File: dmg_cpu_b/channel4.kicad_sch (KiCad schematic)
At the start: 104 parts

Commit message: Further fixes made based on raised issues.
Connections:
- net CH4_EG_STOP: now also EROX.2 (~{Q}); no longer EROX.3 (Q)
- net CH4_FEN renamed CH4_FDIS
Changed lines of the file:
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@@
   (junction (at 201.93 281.305) (diameter 0) (color 0 0 0 0)
   )
-  (no_connect (at 403.86 163.195))
+  (no_connect (at 403.86 158.115))
   (no_connect (at 378.46 163.195))
   (no_connect (at 168.91 276.86))
@@
     (stroke (width 0) (type default) (color 0 0 0 0))
   )
-  (wire (pts (xy 403.86 158.115) (xy 406.4 158.115))
+  (wire (pts (xy 403.86 163.195) (xy 406.4 163.195))
     (stroke (width 0) (type default) (color 0 0 0 0))
   )
@@
     (stroke (width 0) (type default) (color 0 0 0 0))
   )
-  (wire (pts (xy 406.4 158.115) (xy 406.4 135.255))
+  (wire (pts (xy 406.4 135.255) (xy 406.4 163.195))
     (stroke (width 0) (type default) (color 0 0 0 0))
   )
@@
     (effects (font (size 1.27 1.27)) (justify right))
   )
-  (hierarchical_label "CH4_FEN" (shape input) (at 25.4 208.915 180)
+  (hierarchical_label "CH4_FDIS" (shape input) (at 25.4 208.915 180)
     (effects (font (size 1.27 1.27)) (justify right))
   )

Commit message: Fixes made based on raised issues (in APU sheets).
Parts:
- added GYBA: INVERTER_A, symbol DMG_CPU_Cells:INVERTER_A
- renumbered DEMA to DEMO
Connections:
- net CH4_1MHz: now also GYBA.1; no longer GARY.1 (CLK)
- net CH4_EG_STOP: now also EROX.3 (Q); no longer EROX.2 (~{Q})
- net ~{FF21_D0}: no longer JYCO.5 (D)
- net ~{FF21_D1}: no longer JYRE.5 (D)
- net ~{FF21_D2}: no longer JYFU.5 (D)
- net at EVUR.1: now also DARO.6; no longer DUBO.2
- net at EVUR.2: now also DUBO.2; no longer DARO.6
- new net: GARY.1 (CLK), GYBA.2
- new net ~{FF22_D0}: JYCO.5 (D)
- new net ~{FF22_D1}: JYRE.5 (D)
- new net ~{FF22_D2}: JYFU.5 (D)
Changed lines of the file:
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@@
   (junction (at 193.04 214.63) (diameter 0) (color 0 0 0 0)
   )
-  (junction (at 128.905 192.405) (diameter 0) (color 0 0 0 0)
-  )
   (junction (at 377.19 81.28) (diameter 0) (color 0 0 0 0)
   )
@@
   (junction (at 80.645 224.155) (diameter 0) (color 0 0 0 0)
   )
+  (junction (at 114.935 184.15) (diameter 0) (color 0 0 0 0)
+  )
   (junction (at 198.12 137.16) (diameter 0) (color 0 0 0 0)
   )
@@
   (junction (at 201.93 281.305) (diameter 0) (color 0 0 0 0)
   )
-  (no_connect (at 403.86 158.115))
+  (no_connect (at 403.86 163.195))
   (no_connect (at 378.46 163.195))
   (no_connect (at 168.91 276.86))
@@
     (stroke (width 0) (type default) (color 0 0 0 0))
   )
-  (wire (pts (xy 403.86 163.195) (xy 406.4 163.195))
+  (wire (pts (xy 403.86 158.115) (xy 406.4 158.115))
     (stroke (width 0) (type default) (color 0 0 0 0))
   )
@@
     (stroke (width 0) (type default) (color 0 0 0 0))
   )
-  (wire (pts (xy 406.4 135.255) (xy 406.4 163.195))
+  (wire (pts (xy 406.4 135.255) (xy 406.4 158.115))
     (stroke (width 0) (type default) (color 0 0 0 0))
   )
-  (wire (pts (xy 131.445 206.375) (xy 128.905 206.375))
+  (wire (pts (xy 131.445 206.375) (xy 130.175 206.375))
     (stroke (width 0) (type default) (color 0 0 0 0))
   )
@@
     (stroke (width 0) (type default) (color 0 0 0 0))
   )
+  (wire (pts (xy 114.935 184.15) (xy 114.935 197.485))
+    (stroke (width 0) (type default) (color 0 0 0 0))
+  )
   (wire (pts (xy 203.2 132.08) (xy 205.74 132.08))
     (stroke (width 0) (type default) (color 0 0 0 0))
@@
     (stroke (width 0) (type default) (color 0 0 0 0))
   )
-  (wire (pts (xy 128.905 192.405) (xy 156.845 192.405))
-    (stroke (width 0) (type default) (color 0 0 0 0))
-  )
   (wire (pts (xy 84.455 238.76) (xy 59.055 238.76))
     (stroke (width 0) (type default) (color 0 0 0 0))
@@
     (stroke (width 0) (type default) (color 0 0 0 0))
   )
+  (wire (pts (xy 114.935 184.15) (xy 156.845 184.15))
+    (stroke (width 0) (type default) (color 0 0 0 0))
+  )
   (wire (pts (xy 62.23 274.32) (xy 62.23 281.305))
     (stroke (width 0) (type default) (color 0 0 0 0))
@@
     (stroke (width 0) (type default) (color 0 0 0 0))
   )
+  (wire (pts (xy 156.845 184.15) (xy 156.845 192.405))
+    (stroke (width 0) (type default) (color 0 0 0 0))
+  )
   (wire (pts (xy 309.88 180.34) (xy 314.96 180.34))
     (stroke (width 0) (type default) (color 0 0 0 0))
@@
     (stroke (width 0) (type default) (color 0 0 0 0))
   )
-  (wire (pts (xy 128.905 192.405) (xy 125.095 192.405))
+  (wire (pts (xy 113.665 184.15) (xy 114.935 184.15))
     (stroke (width 0) (type default) (color 0 0 0 0))
   )
@@
     (stroke (width 0) (type default) (color 0 0 0 0))
   )
+  (wire (pts (xy 116.205 197.485) (xy 114.935 197.485))
+    (stroke (width 0) (type default) (color 0 0 0 0))
+  )
   (wire (pts (xy 136.525 67.31) (xy 136.525 93.345))
     (stroke (width 0) (type default) (color 0 0 0 0))
@@
     (stroke (width 0) (type default) (color 0 0 0 0))
   )
-  (wire (pts (xy 128.905 206.375) (xy 128.905 192.405))
+  (wire (pts (xy 130.175 206.375) (xy 130.175 197.485))
     (stroke (width 0) (type default) (color 0 0 0 0))
   )
@@
     (stroke (width 0) (type default) (color 0 0 0 0))
   )
+  (wire (pts (xy 130.175 197.485) (xy 128.905 197.485))
+    (stroke (width 0) (type default) (color 0 0 0 0))
+  )
   (wire (pts (xy 123.825 28.575) (xy 123.825 33.02))
     (stroke (width 0) (type default) (color 0 0 0 0))
@@
     (effects (font (size 1.27 1.27)) (justify left bottom))
   )
-  (label "~{FF21_D0}" (at 67.945 226.695 0)
+  (label "~{FF22_D0}" (at 67.945 226.695 0)
     (effects (font (size 1.27 1.27)) (justify left bottom))
   )
@@
     (effects (font (size 1.27 1.27)) (justify left bottom))
   )
-  (label "~{FF21_D1}" (at 67.945 209.55 0)
+  (label "~{FF22_D1}" (at 67.945 209.55 0)
     (effects (font (size 1.27 1.27)) (justify left bottom))
   )
@@
     (effects (font (size 1.27 1.27)) (justify left bottom))
   )
-  (label "~{FF21_D2}" (at 69.215 192.405 0)
+  (label "~{FF22_D2}" (at 69.215 192.405 0)
     (effects (font (size 1.27 1.27)) (justify left bottom))
   )
@@
     (effects (font (size 1.27 1.27)) (justify right))
   )
-  (hierarchical_label "~{FF22_D[0..7]}" (shape input) (at 170.815 129.54 180)
+  (hierarchical_label "~{FF22_D[0..6]}" (shape input) (at 170.815 129.54 180)
     (effects (font (size 1.27 1.27)) (justify right))
   )
-  (hierarchical_label "CH4_1MHz" (shape input) (at 125.095 192.405 180)
+  (hierarchical_label "CH4_1MHz" (shape input) (at 113.665 184.15 180)
     (effects (font (size 1.27 1.27)) (justify right))
   )
@@
     (pin "6")
   )
-  (symbol (lib_id "DMG_CPU_Cells:OR_2") (at 350.52 163.195 0) (unit 1)
+  (symbol (lib_id "DMG_CPU_Cells:OR_2") (at 350.52 163.195 0) (mirror x) (unit 1)
     (in_bom yes) (on_board yes) (fields_autoplaced)
     (property "Reference" "EVUR" (id 0) (at 350.5198 155.6852 0))
@@
       (effects (font (size 1.27 1.27)) hide)
     )
-    (property "Datasheet" "http://iceboy.a-singer.de/doc/dmg_cells.html#or2" (id 3) (at 350.52 170.815 0)
+    (property "Datasheet" "http://iceboy.a-singer.de/doc/dmg_cells.html#or2" (id 3) (at 350.52 155.575 0)
       (effects (font (size 1.27 1.27)) hide)
     )
@@
   (symbol (lib_id "DMG_CPU_Cells:DFFR_B2") (at 121.285 95.885 0) (unit 1)
     (in_bom yes) (on_board yes) (fields_autoplaced)
-    (property "Reference" "DEMA" (id 0) (at 121.285 87.8672 0))
+    (property "Reference" "DEMO" (id 0) (at 121.285 87.8672 0))
     (property "Value" "DFFR_B2" (id 1) (at 121.285 90.4041 0))
     (property "Footprint" "" (id 2) (at 121.285 95.885 0)
@@
     (pin "4")
   )
+  (symbol (lib_id "DMG_CPU_Cells:INVERTER_A") (at 122.555 197.485 0) (unit 1)
+    (in_bom yes) (on_board yes)
+    (property "Reference" "GYBA" (id 0) (at 122.555 189.9752 0))
+    (property "Value" "INVERTER_A" (id 1) (at 122.555 192.5121 0))
+    (property "Footprint" "" (id 2) (at 120.015 197.485 0)
+      (effects (font (size 1.27 1.27)) hide)
+    )
+    (property "Datasheet" "http://iceboy.a-singer.de/doc/dmg_cells.html#inv_a" (id 3) (at 123.825 205.105 0)
+      (effects (font (size 1.27 1.27)) hide)
+    )
+    (pin "1")
+    (pin "2")
+  )
   (symbol (lib_id "DMG_CPU_Cells:INVERTER_A") (at 25.4 271.78 0) (unit 1)

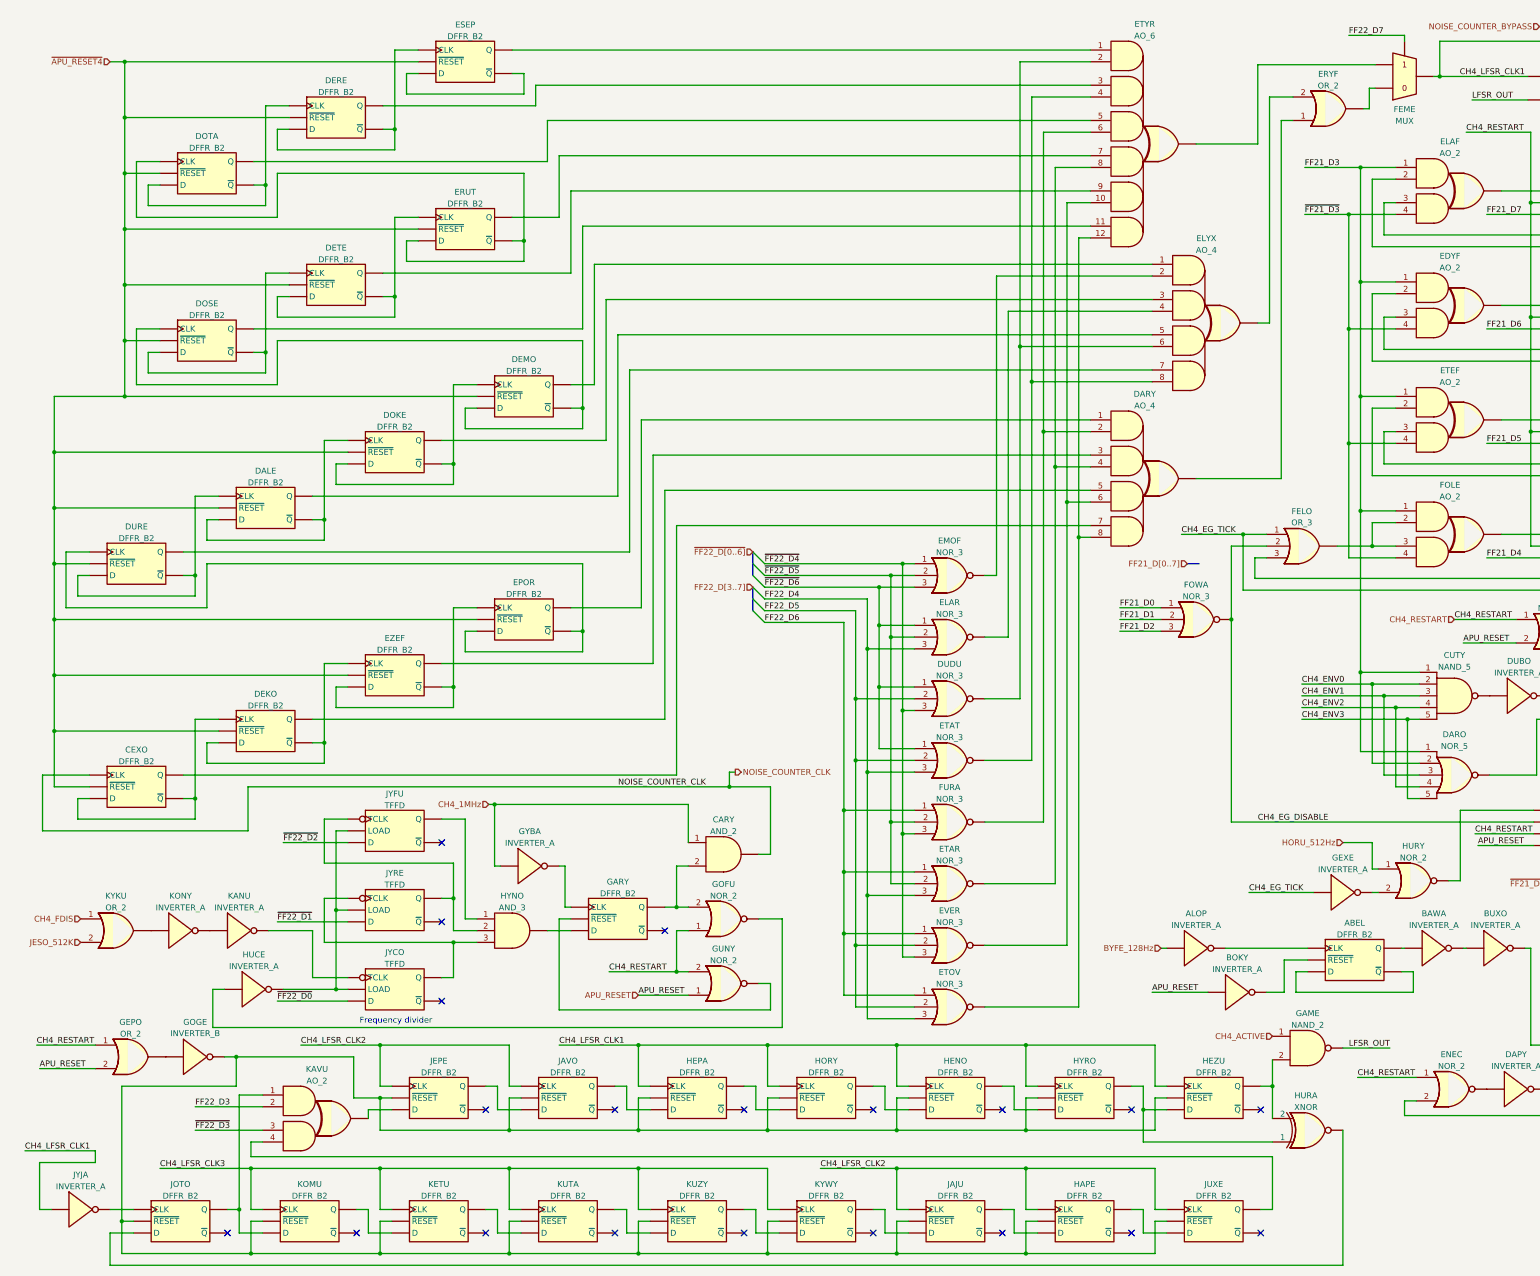
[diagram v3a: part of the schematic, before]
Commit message: Some mistakes found in APU sheets, notes added for clarity. Edit in PPU sheets following review.
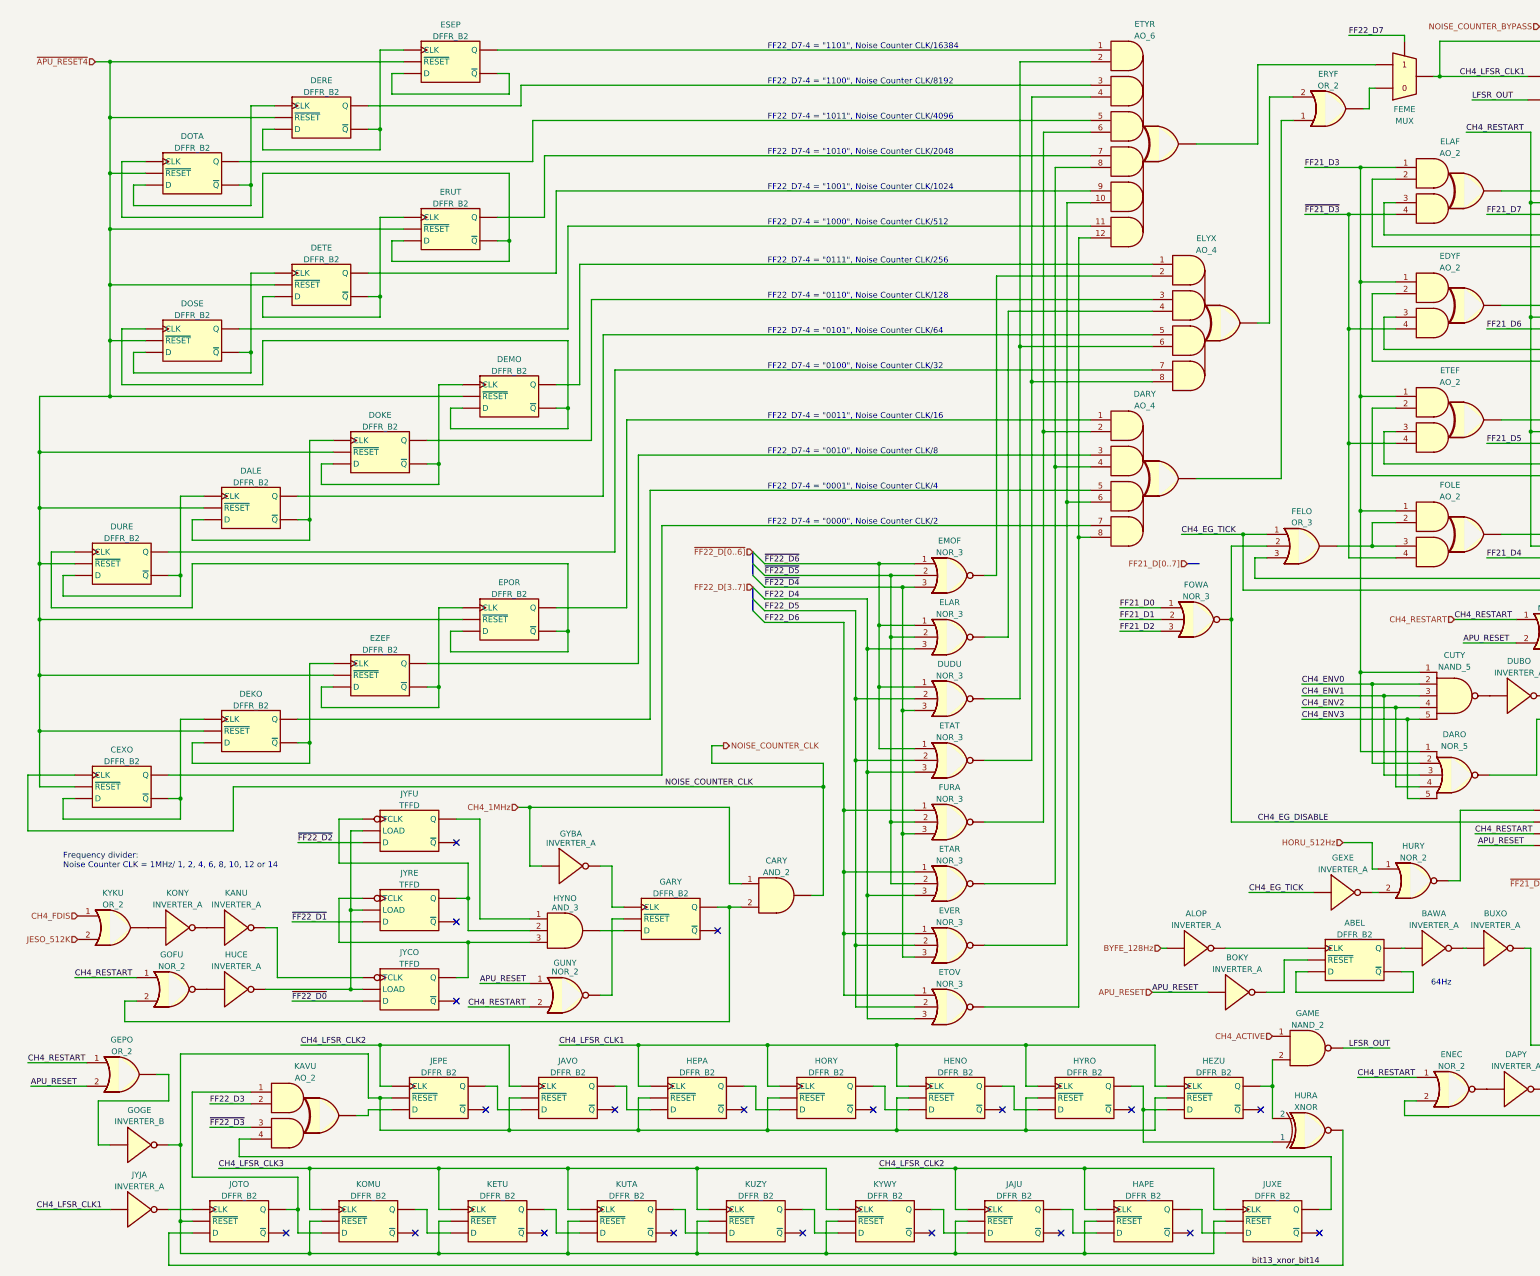
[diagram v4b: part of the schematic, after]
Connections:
- net ~{FF22_D4}: now also EMOF.3; no longer EMOF.1
- net ~{FF22_D6}: now also EMOF.1; no longer EMOF.3
- net bit13_xnor_bit14: now reaches HURA.1, JOTO.3 (D)
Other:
- note added: "64Hz"
- note added: "FF22_D7-4 = "0000", Noise Counter CLK/2"
- note added: "FF22_D7-4 = "0001", Noise Counter CLK/4"
- note added: "FF22_D7-4 = "0010", Noise Counter CLK/8"
- note added: "FF22_D7-4 = "0011", Noise Counter CLK/16"
- note added: "FF22_D7-4 = "0100", Noise Counter CLK/32"
- note added: "FF22_D7-4 = "0101", Noise Counter CLK/64"
- note added: "FF22_D7-4 = "0110", Noise Counter CLK/128"
- note added: "FF22_D7-4 = "0111", Noise Counter CLK/256"
- note added: "FF22_D7-4 = "1000", Noise Counter CLK/512"
- note added: "FF22_D7-4 = "1001", Noise Counter CLK/1024"
- note added: "FF22_D7-4 = "1010", Noise Counter CLK/2048"
- note added: "FF22_D7-4 = "1011", Noise Counter CLK/4096"
- note added: "FF22_D7-4 = "1100", Noise Counter CLK/8192"
- note added: "FF22_D7-4 = "1101", Noise Counter CLK/16384"
- note added: "Frequency divider: Noise Counter CLK = 1MHz/ 1, 2, 4, 6, 8, 10, 12 or 14"
- note removed: "Frequency divider"
- moved on the sheet: CARY, CEXO, DALE, DEKO, DEMO, DERE, DETE, DOKE, DOSE, DOTA, DURE, EPOR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

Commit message: VRAM interface sheet added but various edits in existing sheets. Notable merge of RESET, CLOCKS and FF04 DIV sheets
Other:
- company: (none) -> CC-BY-SA-4.0 Régis Galland & Michael Singer -- Derived work from Furrtek
- title: (none) -> DMG CPU B
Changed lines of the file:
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@@
 (kicad_sch (version 20211123) (generator eeschema)
   (paper "A3")
+  (title_block
+    (title "DMG CPU B")
+    (date "2022-05-02")
+    (rev "0")
+    (company "CC-BY-SA-4.0 Régis Galland & Michael Singer -- Derived work from Furrtek")
+    (comment 1 "https://github.com/msinger/dmg-schematics")
+  )
   (junction (at 200.66 134.62) (diameter 0) (color 0 0 0 0)
   )

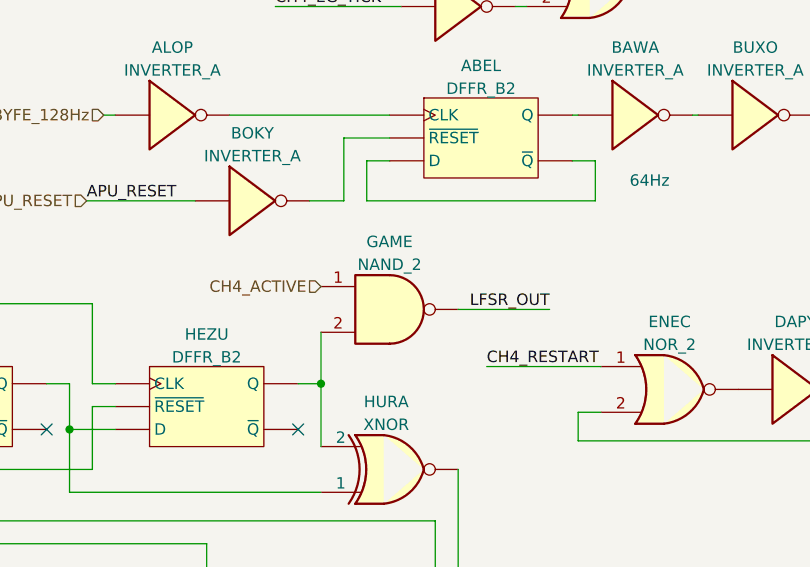
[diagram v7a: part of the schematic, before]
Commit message: Fix done based on github tickets #152 to #155
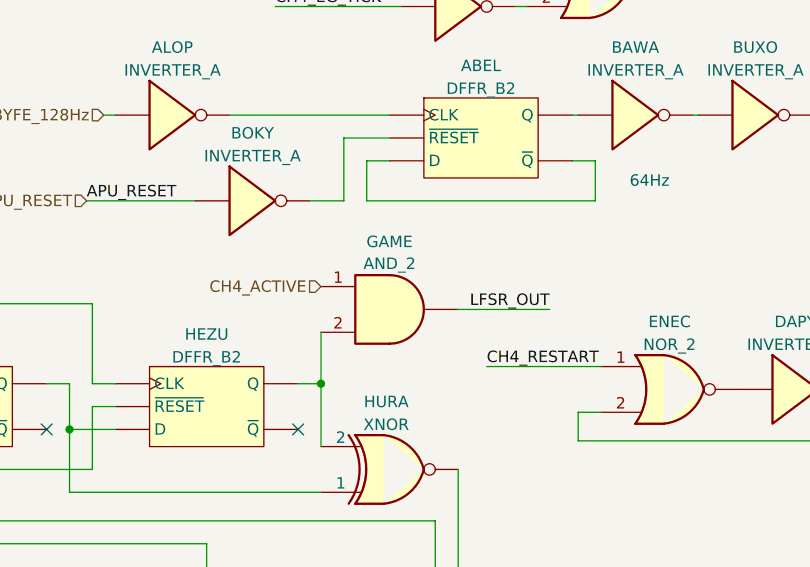
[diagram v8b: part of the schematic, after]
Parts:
- GAME: value NAND_2 -> AND_2; symbol DMG_CPU_Cells:NAND_2 -> DMG_CPU_Cells:AND_2
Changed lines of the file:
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@@
     (pin "4")
   )
-  (symbol (lib_id "DMG_CPU_Cells:NAND_2") (at 290.83 236.855 0) (unit 1)
-    (in_bom yes) (on_board yes) (fields_autoplaced)
+  (symbol (lib_id "DMG_CPU_Cells:AND_2") (at 290.83 236.855 0) (unit 1)
+    (in_bom yes) (on_board yes)
     (property "Reference" "GAME" (id 0) (at 290.83 229.3452 0))
-    (property "Value" "NAND_2" (id 1) (at 290.83 231.8821 0))
+    (property "Value" "AND_2" (id 1) (at 290.83 231.775 0))
     (property "Footprint" "" (id 2) (at 290.83 236.855 0)
       (effects (font (size 1.27 1.27)) hide)
     )
-    (property "Datasheet" "http://iceboy.a-singer.de/doc/dmg_cells.html#nand2" (id 3) (at 290.83 244.475 0)
+    (property "Datasheet" "http://iceboy.a-singer.de/doc/dmg_cells.html#and2" (id 3) (at 290.83 244.475 0)
       (effects (font (size 1.27 1.27)) hide)
     )
